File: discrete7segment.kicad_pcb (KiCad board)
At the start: 2 copper layers, 76 parts, among them P1 CONN_01X02, Q1 Q_NPN_BEC, Q2 Q_NPN_BEC, Q3 Q_NPN_BEC, Q4 Q_NPN_BEC, Q5 Q_NPN_BEC, Q6 Q_NPN_BEC, Q7 Q_NPN_BEC, U1 555, U2 4017

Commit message: done digit
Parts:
- moved D57 111.9 mm to (116.8, 144.8), turned to 270 degrees
- moved D50 103.3 mm to (116.8, 137.2), turned to 270 degrees
- moved D58 98.1 mm to (132.1, 129.5)
- moved D56 74.7 mm to (139.7, 137.2), turned to 270 degrees
- moved D62 69.1 mm to (132.1, 152.4)
- moved D51 67.5 mm to (124.5, 129.5)
- moved D54 67.3 mm to (147.3, 152.4)
- moved D63 65.9 mm to (139.7, 144.8), turned to 270 degrees
- moved D59 63.7 mm to (154.9, 129.5)
- moved D52 53.2 mm to (147.3, 129.5)
- moved D55 48.9 mm to (124.5, 152.4)
- moved D60 48.6 mm to (162.6, 144.8), turned to 270 degrees
- moved D61 40.7 mm to (154.9, 152.4)
- moved D53 21.7 mm to (162.6, 137.2), turned to 270 degrees
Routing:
- net GND: track 18.1 -> 194.5 mm, vias 5 -> 6
- net +5V: track 5.23 -> 115.9 mm, vias 0 -> 2
- net Net-(D55-Pad1): track 0.00 -> 63.9 mm, vias 0 -> 4
- net Net-(D16-Pad2): track 15.2 -> 70.2 mm, vias 2 -> 4
- net Net-(D12-Pad2): track 69.8 -> 119.2 mm, vias 6 -> 10
- net Net-(D56-Pad1): track 0.00 -> 43.3 mm, vias 0 -> 4
- net Net-(D54-Pad1): track 0.00 -> 38.4 mm, vias 0 -> 2
- net Net-(D1-Pad2): track 84.5 -> 121.8 mm, vias 8 -> 12
- net Net-(D11-Pad2): track 84.9 -> 120.2 mm, vias 8 -> 10
- net Net-(D53-Pad1): track 0.00 -> 32.6 mm
- net Net-(D52-Pad1): track 0.00 -> 24.6 mm
- net Net-(D50-Pad1): track 0.00 -> 23.7 mm
- net Net-(D20-Pad2): track 86.3 -> 108.5 mm, vias 10 -> 12
- net Net-(D19-Pad2): track 84.7 -> 106.4 mm
- net Net-(D15-Pad2): track 74.2 -> 95.8 mm
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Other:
- board text removed: "Now shape 8 from the LEDs and that'll be it."

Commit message: board finished
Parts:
- moved P1 9.25 mm to (78.7, 71.1), turned to 0 degrees
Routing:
- net +5V: track 115.9 -> 128.7 mm, vias 2 -> 4
- net GND: track 194.5 -> 201.0 mm, vias 6 -> 7
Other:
- board outline added: 111.8 x 94 mm
- board text added: "+5V"
- board text added: "-"
- board text added: "0"
- board text added: "1"
- board text added: "2"
- board text added: "3"
- board text added: "4"
- board text added: "5"
- board text added: "6"
- board text added: "7"
- board text added: "8"
- board text added: "9"
- board text added: "a"
- board text added: "b"
- board text added: "c"
- board text added: "d"
- board text added: "e"
- board text added: "f"
- board text added: "g"
- board text removed: "And so on and so forth.."

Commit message: found bugs, needs rework
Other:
- board text added: "TODO: Move chips above the display and save space"
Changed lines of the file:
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@@
     (area 68.58 63.424999 182.955001 157.555001)
     (thickness 1.6)
-    (drawings 89)
+    (drawings 90)
     (tracks 551)
     (zones 0)
@@
     )
   )
+  (gr_text "TODO:\nMove chips above the display\nand save space" (at 93.98 134.62) (layer F.SilkS)
+    (effects (font (size 1.5 1.5) (thickness 0.3)))
+  )
   (gr_text g (at 175.26 125.73 90) (layer F.SilkS)

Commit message: layout from scratch
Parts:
- D1, D10, D11, D12, D13, D14, D15, D16, D17, D18, D19, D2, D20, D21, D22, D23, D24, D25, D26, D27, D28, D29, D3, D30, D31, D32, D33, D34, D35, D36, D37, D38, D39, D4, D40, D41, D42, D43, D44, D45, D46, D47, D48, D49, D5, D6, D7, D8, D9: footprint Diodes_SMD:MiniMELF_Handsoldering -> Diodes_SMD:MiniMELF_Standard
- moved D55 87.0 mm to (178.7, 84.4)
- moved D57 83.9 mm to (179.8, 89.3)
- moved Q7 72.7 mm to (108.6, 96.9)
- moved D50 67.6 mm to (171.3, 97.1)
- moved D15 67.1 mm to (162.8, 70.8)
- moved D7 65.2 mm to (151.7, 70.8)
- moved Q6 63.1 mm to (118.7, 76.6)
- moved D61 62.2 mm to (170.7, 92.2)
- moved D51 60.8 mm to (176.3, 97.7)
- moved D36 59.6 mm to (106.9, 105.2)
- moved D1 58.3 mm to (157.3, 70.8)
- moved U1 56.7 mm to (133.9, 68.9)
- moved Q5 56.7 mm to (125.5, 69.5)
- moved D23 56.4 mm to (168.2, 78.6)
- moved D54 56.4 mm to (175.0, 103.3)
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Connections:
- D16 pad 1: /c -> /b
- D17 pad 2: Net-(D11-Pad2) -> Net-(D17-Pad2)
- D18 pad 2: Net-(D12-Pad2) -> Net-(D11-Pad2)
- D19 pad 2: Net-(D19-Pad2) -> Net-(D12-Pad2)
- D21 pad 2: Net-(D13-Pad2) -> Net-(D21-Pad2)
- D22 pad 2: Net-(D14-Pad2) -> Net-(D13-Pad2)
- D23 pad 2: Net-(D15-Pad2) -> Net-(D14-Pad2)
- D24 pad 1: /d -> /c
- D24 pad 2: Net-(D1-Pad2) -> Net-(D15-Pad2)
- D25 pad 1: /d -> /c
- D25 pad 2: Net-(D11-Pad2) -> Net-(D16-Pad2)
- D26 pad 2: Net-(D19-Pad2) -> Net-(D1-Pad2)
- D27 pad 2: Net-(D20-Pad2) -> Net-(D11-Pad2)
- D28 pad 2: Net-(D13-Pad2) -> Net-(D20-Pad2)
- D29 pad 2: Net-(D14-Pad2) -> Net-(D21-Pad2)
- D3 pad 2: Net-(D19-Pad2) -> Net-(D20-Pad2)
- D30 pad 2: Net-(D15-Pad2) -> Net-(D14-Pad2)
- D31 pad 1: /e -> /d
- D31 pad 2: Net-(D1-Pad2) -> Net-(D15-Pad2)
- D32 pad 1: /e -> /d
- D32 pad 2: Net-(D20-Pad2) -> Net-(D16-Pad2)
- D33 pad 2: Net-(D13-Pad2) -> Net-(D1-Pad2)
- D34 pad 2: Net-(D14-Pad2) -> Net-(D21-Pad2)
- D35 pad 2: Net-(D15-Pad2) -> Net-(D14-Pad2)
- D36 pad 1: /f -> /e
- D36 pad 2: Net-(D12-Pad2) -> Net-(D16-Pad2)
- D37 pad 2: Net-(D19-Pad2) -> Net-(D12-Pad2)
- D39 pad 2: Net-(D39-Pad2) -> Net-(D21-Pad2)
- D4 pad 2: Net-(D20-Pad2) -> Net-(D21-Pad2)
- D40 pad 2: Net-(D13-Pad2) -> Net-(D14-Pad2)
- D42 pad 1: /g -> /f
- D42 pad 2: Net-(D1-Pad2) -> Net-(D16-Pad2)
- D43 pad 2: Net-(D11-Pad2) -> Net-(D1-Pad2)
- D44 pad 2: Net-(D12-Pad2) -> Net-(D11-Pad2)
- D45 pad 2: Net-(D19-Pad2) -> Net-(D12-Pad2)
- D47 pad 2: Net-(D39-Pad2) -> Net-(D21-Pad2)
- D48 pad 2: Net-(D13-Pad2) -> Net-(D14-Pad2)
- D49 pad 2: Net-(D14-Pad2) -> Net-(D15-Pad2)
- D5 pad 2: Net-(D39-Pad2) -> Net-(D13-Pad2)
- D6 pad 2: Net-(D13-Pad2) -> Net-(D14-Pad2)
- D7 pad 2: Net-(D14-Pad2) -> Net-(D15-Pad2)
- D8 pad 2: Net-(D15-Pad2) -> Net-(D16-Pad2)
- D9 pad 2: Net-(D16-Pad2) -> Net-(D17-Pad2)
- U2 pad 1: Net-(D20-Pad2) -> Net-(D21-Pad2)
- U2 pad 10: Net-(D19-Pad2) -> Net-(D20-Pad2)
- U2 pad 11: Net-(D15-Pad2) -> Net-(D16-Pad2)
- U2 pad 12: Net-(U2-Pad12) -> (no net)
- U2 pad 3: Net-(D16-Pad2) -> Net-(D17-Pad2)
- U2 pad 5: Net-(D39-Pad2) -> Net-(D13-Pad2)
- U2 pad 6: Net-(D13-Pad2) -> Net-(D14-Pad2)
- U2 pad 9: Net-(D14-Pad2) -> Net-(D15-Pad2)
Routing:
- net GND: track 201.0 -> 0.00 mm, vias 7 -> 0
- net +5V: track 128.7 -> 0.00 mm, vias 4 -> 0
- net Net-(D1-Pad2): track 121.8 -> 0.00 mm, vias 12 -> 0
- net Net-(D11-Pad2): track 120.2 -> 0.00 mm, vias 10 -> 0
- net Net-(D12-Pad2): track 119.2 -> 0.00 mm, vias 10 -> 0
- net Net-(D13-Pad2): track 109.4 -> 0.00 mm, vias 14 -> 0
- net Net-(D20-Pad2): track 108.5 -> 0.00 mm, vias 12 -> 0
- net Net-(D19-Pad2): track 106.4 -> 0.00 mm, vias 8 -> 0
- net Net-(D14-Pad2): track 101.4 -> 0.00 mm, vias 10 -> 0
- net Net-(D39-Pad2): track 101.3 -> 0.00 mm, vias 6 -> 0
- net Net-(D15-Pad2): track 95.8 -> 0.00 mm, vias 10 -> 0
- net Net-(D16-Pad2): track 70.2 -> 0.00 mm, vias 4 -> 0
- net Net-(D55-Pad1): track 63.9 -> 0.00 mm, vias 4 -> 0
- net /c: track 50.6 -> 0.00 mm
- net /b: track 50.6 -> 0.00 mm
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- removed copper zone on F.Cu, net +5V
- removed copper zone on B.Cu, net GND
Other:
- board outline removed
- board text removed: "+5V"
- board text removed: "-"
- board text removed: "0"
- board text removed: "1"
- board text removed: "2"
- board text removed: "3"
- board text removed: "4"
- board text removed: "5"
- board text removed: "6"
- board text removed: "7"
- board text removed: "8"
- board text removed: "9"
- board text removed: "TODO: Move chips above the display and save space"
- board text removed: "a"
- board text removed: "b"
- board text removed: "c"
- board text removed: "d"
- board text removed: "e"
- board text removed: "f"
- board text removed: "g"

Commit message: layout finished
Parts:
- moved D55 88.3 mm to (119.4, 149.9)
- moved D57 85.8 mm to (114.3, 144.8)
- moved U1 81.6 mm to (104.1, 144.8)
- moved D50 69.7 mm to (114.3, 137.2)
- moved D15 67.5 mm to (109.2, 111.8)
- moved P1 67.2 mm to (94.0, 147.3), turned to 180 degrees
- moved D51 66.5 mm to (119.4, 132.1)
- moved D7 64.7 mm to (101.6, 111.8)
- moved D61 63.2 mm to (144.8, 149.9)
- moved U2 63.1 mm to (101.6, 134.6), turned to 0 degrees
- moved D42 60.8 mm to (139.7, 116.8)
- moved D54 60.0 mm to (137.2, 149.9)
- moved D23 58.5 mm to (116.8, 106.7)
- moved D1 55.9 mm to (101.6, 76.2)
- moved R2 53.8 mm to (106.7, 151.1), turned to 90 degrees
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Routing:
- net Net-(D1-Pad2): track 0.00 -> 119.7 mm, vias 0 -> 10
- net Net-(D11-Pad2): track 0.00 -> 112.7 mm, vias 0 -> 8
- net Net-(D12-Pad2): track 0.00 -> 111.3 mm, vias 0 -> 8
- net Net-(D20-Pad2): track 0.00 -> 100.8 mm, vias 0 -> 8
- net +5V: track 0.00 -> 99.0 mm, vias 0 -> 6
- net Net-(D21-Pad2): track 0.00 -> 97.2 mm, vias 0 -> 12
- net GND: track 0.00 -> 96.1 mm, vias 0 -> 10
- net Net-(D17-Pad2): track 0.00 -> 92.8 mm, vias 0 -> 2
- net Net-(D14-Pad2): track 0.00 -> 90.6 mm, vias 0 -> 14
- net Net-(D15-Pad2): track 0.00 -> 79.2 mm, vias 0 -> 12
- net Net-(D13-Pad2): track 0.00 -> 74.2 mm, vias 0 -> 4
- net Net-(D16-Pad2): track 0.00 -> 59.4 mm, vias 0 -> 12
- net /b: track 0.00 -> 51.2 mm
- net /c: track 0.00 -> 51.2 mm
- net /a: track 0.00 -> 46.5 mm, vias 0 -> 2
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- added copper zone on F.Cu, net +5V
- added copper zone on B.Cu, net GND
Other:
- board outline added: 61 x 86.4 mm
- board text added: "04/18"
- board text added: "Diode Matrix ROM"
- board text added: "Unregulated Powersupply"

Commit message: new layout initiated
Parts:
- removed D50, D51, D52, D53, D54, D55, D56, D57, D58, D59, D60, D61, D62, D63: LED, LEDs:LED_0805
- added C2: 1uF, Capacitors_ThroughHole:C_Radial_D5_L6_P2.5, F.Cu at (152.8, 139.1)
- added P2: CLK, Pin_Headers:Pin_Header_Straight_1x01, F.Cu at (196.1, 113.2)
- added P3: CONN_01X10, Pin_Headers:Pin_Header_Straight_1x10, F.Cu at (144.7, 94.3)
- added R3: 330, Resistors_ThroughHole:Resistor_Vertical_RM5mm, F.Cu at (156.3, 128.8)
- added R4: 330, Resistors_ThroughHole:Resistor_Vertical_RM5mm, F.Cu at (174.6, 118.9)
- added R5: 330, Resistors_ThroughHole:Resistor_Vertical_RM5mm, F.Cu at (202.4, 92.5)
- added R6: 330, Resistors_ThroughHole:Resistor_Vertical_RM5mm, F.Cu at (165.4, 118.9)
- added R7: 330, Resistors_ThroughHole:Resistor_Vertical_RM5mm, F.Cu at (156.3, 118.9)
- added R8: 330, Resistors_ThroughHole:Resistor_Vertical_RM5mm, F.Cu at (172.3, 109.1)
- added R9: 330, Resistors_ThroughHole:Resistor_Vertical_RM5mm, F.Cu at (183.2, 103.1)
- added SW1: SPDT, Buttons_Switches_ThroughHole:SW_Micro_SPST, F.Cu at (207.0, 101.6)
- added U3: 78L05, TO_SOT_Packages_THT:TO-92_Inline_Narrow_Oval, F.Cu at (189.9, 112.7)
- added U4: 7-seg_1-dig, Displays_7-Segment:7SegmentLED_LTS6760_LTS6780, F.Cu at (160.5, 98.1)
- C1: footprint Capacitors_SMD:C_1206_HandSoldering -> Capacitors_ThroughHole:C_Radial_D5_L6_P2.5
- D1, D10, D11, D12, D13, D14, D15, D16, D17, D18, D19, D2, D20, D21, D22, D23, D24, D25, D26, D27, D28, D29, D3, D30, D31, D32, D33, D34, D35, D36, D37, D38, D39, D4, D40, D41, D42, D43, D44, D45, D46, D47, D48, D49, D5, D6, D7, D8, D9: footprint Diodes_SMD:MiniMELF_Standard -> Diodes_ThroughHole:Diode_DO-41_SOD81_Vertical_KathodeUp
- Q1, Q2, Q3, Q4, Q5, Q6, Q7: value Q_NPN_BEC -> Q_NPN_CBE; footprint TO_SOT_Packages_SMD:SOT-23_Handsoldering -> TO_SOT_Packages_THT:TO-92_Inline_Narrow_Oval
- R1, R2: footprint Resistors_SMD:R_0805_HandSoldering -> Resistors_ThroughHole:Resistor_Vertical_RM5mm
- U1: footprint SMD_Packages:SOIC-8-N -> Housings_DIP:DIP-8_W7.62mm_LongPads
- U2: footprint SMD_Packages:SO-16-N -> Housings_DIP:DIP-16_W7.62mm_LongPads
- moved D10 141.3 mm to (239.2, 131.5), turned to 0 degrees
- moved D9 140.7 mm to (232.2, 139.5), turned to 0 degrees
- moved D7 140.2 mm to (239.0, 139.5), turned to 0 degrees
- moved D6 138.7 mm to (240.1, 99.9), turned to 0 degrees
- moved D12 131.0 mm to (232.2, 131.5), turned to 0 degrees
- moved D13 130.4 mm to (237.8, 123.6), turned to 0 degrees
- moved D11 129.9 mm to (225.4, 139.5), turned to 0 degrees
- moved D16 128.2 mm to (237.4, 115.7), turned to 0 degrees
- moved D22 121.1 mm to (237.6, 91.9), turned to 0 degrees
- moved D8 117.7 mm to (218.2, 132.7), turned to 0 degrees
- moved D15 117.7 mm to (225.2, 131.5), turned to 0 degrees
- moved D17 117.3 mm to (211.4, 140.6), turned to 0 degrees
- moved D19 117.3 mm to (233.3, 99.9), turned to 0 degrees
- moved D14 114.3 mm to (218.4, 140.6), turned to 0 degrees
- moved D2 112.5 mm to (212.3, 101.0), turned to 0 degrees
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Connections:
- net Net-(D1-Pad2) renamed /2
- net Net-(D11-Pad2) renamed /3
- net Net-(D12-Pad2) renamed /4
- net Net-(D13-Pad2) renamed /7
- net Net-(D14-Pad2) renamed /8
- net Net-(D15-Pad2) renamed /9
- net Net-(D16-Pad2) renamed /0
- net Net-(D17-Pad2) renamed /1
- net Net-(D20-Pad2) renamed /5
- net Net-(D21-Pad2) renamed /6
- P1 pad 1: +5V -> Net-(C2-Pad1)
- Q1 pad 1: /a -> +5V
- Q1 pad 2: Net-(D50-Pad1) -> /a
- Q1 pad 3: +5V -> Net-(Q1-Pad3)
- Q2 pad 1: /b -> +5V
- Q2 pad 2: Net-(D51-Pad1) -> /b
- Q2 pad 3: +5V -> Net-(Q2-Pad3)
- Q3 pad 1: /c -> +5V
- Q3 pad 2: Net-(D52-Pad1) -> /c
- Q3 pad 3: +5V -> Net-(Q3-Pad3)
- Q4 pad 1: /d -> +5V
- Q4 pad 2: Net-(D53-Pad1) -> /d
- Q4 pad 3: +5V -> Net-(Q4-Pad3)
- Q5 pad 1: /e -> +5V
- Q5 pad 2: Net-(D54-Pad1) -> /e
- Q5 pad 3: +5V -> Net-(Q5-Pad3)
- Q6 pad 1: /f -> +5V
- Q6 pad 2: Net-(D55-Pad1) -> /f
- Q6 pad 3: +5V -> Net-(Q6-Pad3)
- Q7 pad 1: /g -> +5V
- Q7 pad 2: Net-(D56-Pad1) -> /g
- Q7 pad 3: +5V -> Net-(Q7-Pad3)
- U1 pad 3: Net-(U1-Pad3) -> Net-(SW1-Pad1)
- U1 pad 5: GND -> (no net)
- U2 pad 14: Net-(U1-Pad3) -> Net-(P2-Pad1)
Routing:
- net /2: track 119.7 -> 0.00 mm, vias 10 -> 0
- net /3: track 112.7 -> 0.00 mm, vias 8 -> 0
- net /4: track 111.3 -> 0.00 mm, vias 8 -> 0
- net /5: track 100.8 -> 0.00 mm, vias 8 -> 0
- net +5V: track 99.0 -> 0.00 mm, vias 6 -> 0
- net /6: track 97.2 -> 0.00 mm, vias 12 -> 0
- net GND: track 96.1 -> 0.00 mm, vias 10 -> 0
- net /1: track 92.8 -> 0.00 mm, vias 2 -> 0
- net /8: track 90.6 -> 0.00 mm, vias 14 -> 0
- net /9: track 79.2 -> 0.00 mm, vias 12 -> 0
- net /7: track 74.2 -> 0.00 mm, vias 4 -> 0
- net /0: track 59.4 -> 0.00 mm, vias 12 -> 0
- net /b: track 51.2 -> 0.00 mm
- net /c: track 51.2 -> 0.00 mm
- net /a: track 46.5 -> 0.00 mm, vias 2 -> 0
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- removed copper zone on F.Cu, net +5V
- removed copper zone on B.Cu, net GND
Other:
- board outline removed
- board text removed: "04/18"
- board text removed: "Diode Matrix ROM"
- board text removed: "Unregulated Powersupply"

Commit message: layout done
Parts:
- R1, R2, R3, R4, R5, R6, R7, R8, R9: footprint Resistors_ThroughHole:Resistor_Vertical_RM5mm -> Resistors_ThroughHole:Resistor_Horizontal_RM7mm
- moved SW1 132.8 mm to (76.2, 124.5), turned to 270 degrees
- moved D6 125.7 mm to (116.8, 124.5), turned to 180 degrees
- moved D7 122.6 mm to (116.8, 129.5), turned to 180 degrees
- moved R2 122.0 mm to (73.7, 116.8), turned to 90 degrees
- moved P2 121.8 mm to (76.2, 134.6)
- moved D10 120.7 mm to (124.5, 94.0), turned to 180 degrees
- moved D9 119.0 mm to (124.5, 88.9), turned to 180 degrees
- moved D16 114.5 mm to (124.5, 134.6), turned to 180 degrees
- moved C1 113.5 mm to (76.2, 101.6)
- moved D13 113.4 mm to (124.5, 119.4), turned to 180 degrees
- moved P1 111.9 mm to (71.1, 88.9)
- moved D12 111.2 mm to (124.5, 104.1), turned to 180 degrees
- moved D22 109.0 mm to (132.1, 119.4), turned to 180 degrees
- moved D11 108.7 mm to (124.5, 99.1), turned to 180 degrees
- moved U3 103.8 mm to (88.9, 88.9), turned to 180 degrees
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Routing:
- net Net-(R1-Pad2): track 0.00 -> 35.4 mm
- net /1: track 0.00 -> 28.9 mm
- net Net-(P2-Pad1): track 0.00 -> 28.6 mm
- net Net-(SW1-Pad1): track 0.00 -> 28.4 mm
- net /2: track 0.00 -> 26.8 mm, vias 0 -> 2
- net Net-(C1-Pad1): track 0.00 -> 26.0 mm
- net Net-(C2-Pad1): track 0.00 -> 19.9 mm
- added copper zone on F.Cu, net +5V
- added copper zone on B.Cu, net GND
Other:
- board outline added: 99.1 x 76.2 mm

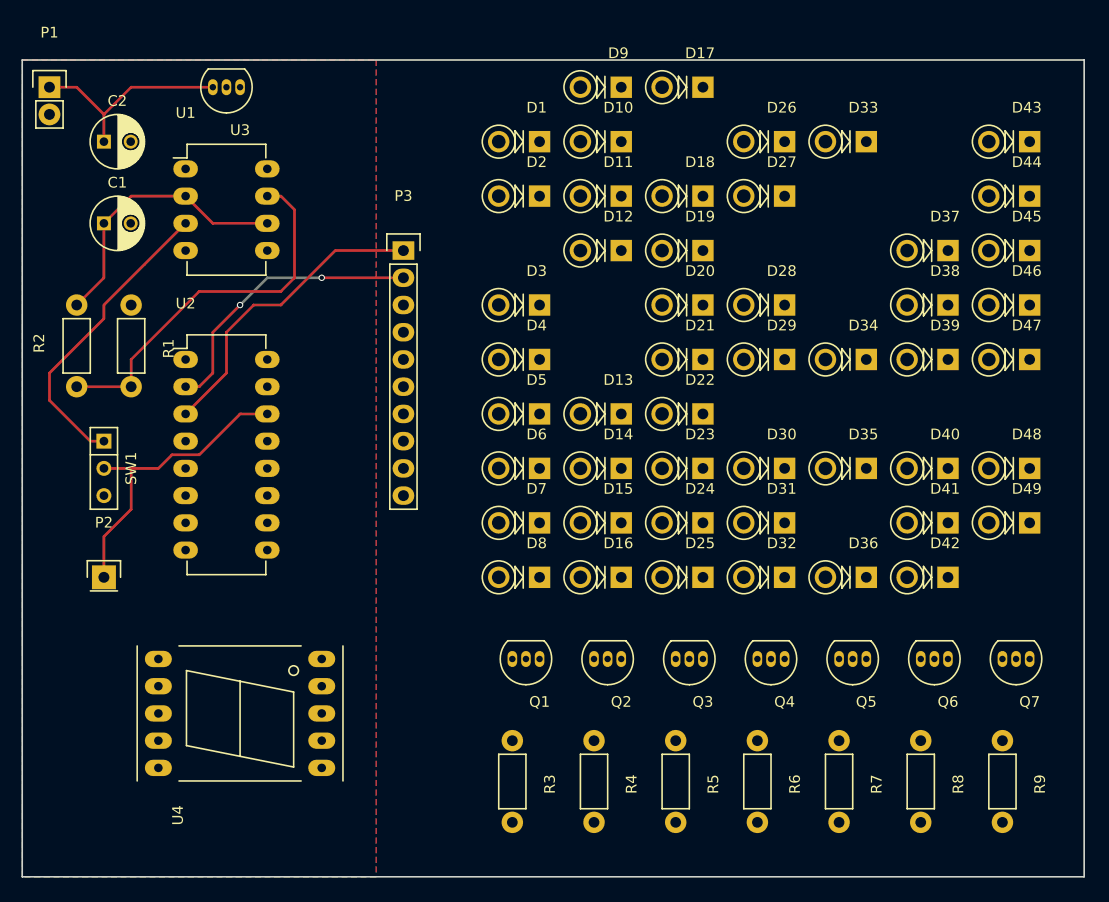
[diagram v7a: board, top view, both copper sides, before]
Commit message: through hole layout
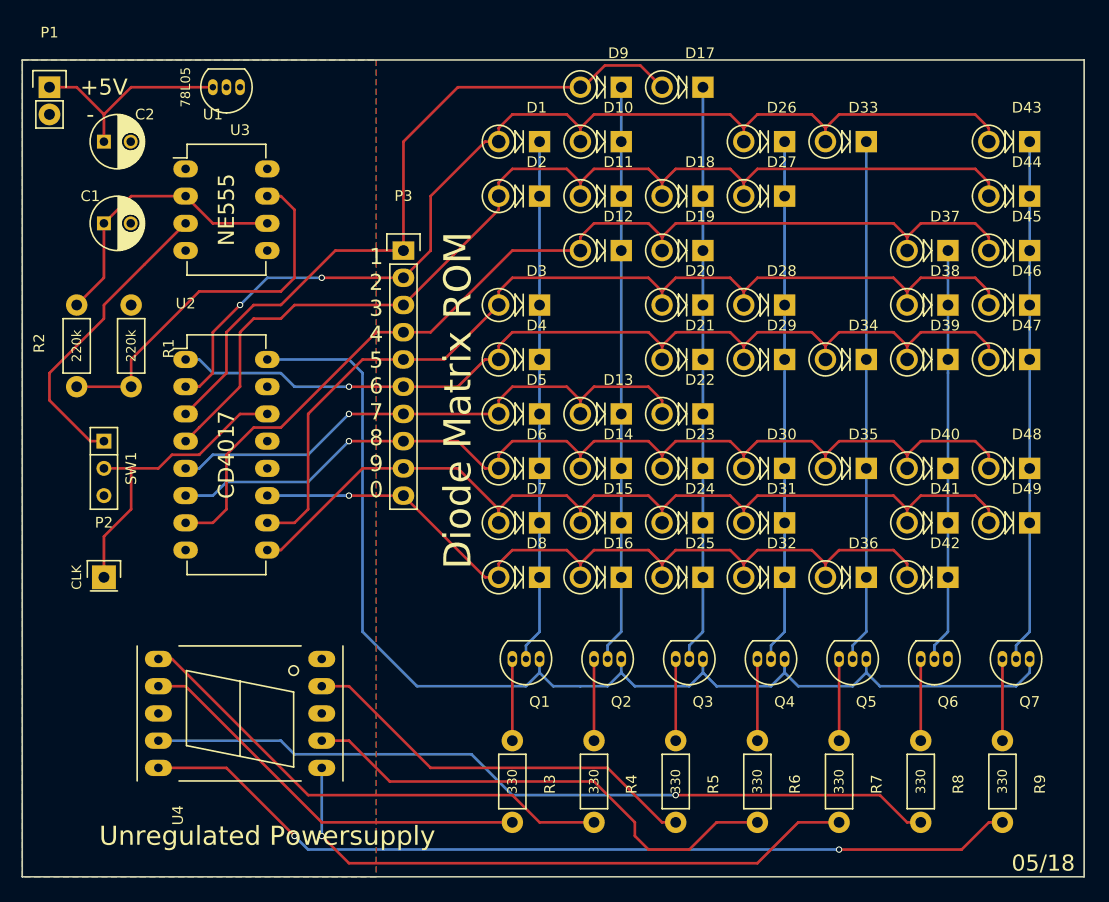
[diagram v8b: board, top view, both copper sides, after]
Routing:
- net +5V: track 0.00 -> 111.3 mm
- net /3: track 0.00 -> 98.7 mm
- net /4: track 0.00 -> 96.7 mm
- net /8: track 0.00 -> 93.3 mm, vias 0 -> 1
- net /5: track 0.00 -> 91.5 mm
- net /6: track 0.00 -> 89.9 mm, vias 0 -> 1
- net /9: track 0.00 -> 86.2 mm
- net Net-(R9-Pad2): track 0.00 -> 82.9 mm, vias 0 -> 2
- net /0: track 0.00 -> 75.7 mm, vias 0 -> 1
- net Net-(R8-Pad2): track 0.00 -> 74.3 mm, vias 0 -> 1
- net /2: track 26.8 -> 100.2 mm
- net Net-(R7-Pad2): track 0.00 -> 57.2 mm, vias 0 -> 1
- net /c: track 0.00 -> 53.9 mm
- net /b: track 0.00 -> 53.9 mm
- net /7: track 0.00 -> 52.5 mm, vias 0 -> 1
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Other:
- board text added: "+5V"
- board text added: "-"
- board text added: "05/18"
- board text added: "1 2 3 4 5 6 7 8 9 0"
- board text added: "220k"
- board text added: "330"
- board text added: "78L05"
- board text added: "CD4017"
- board text added: "CLK"
- board text added: "Diode Matrix ROM"
- board text added: "NE555"
- board text added: "Unregulated Powersupply"
